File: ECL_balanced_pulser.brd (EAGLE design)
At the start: 40 x 50 mm, 41 parts, among them Q1 BC636, T1 2N2369, U1 MC100EPT22DG, U2 MAX961ESA+, X1 BU-SMA-H, X2 BU-SMA-H, X3 BU-SMA-H

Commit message: added a small copyright note
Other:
- board text added: "Copyright 2015 by Mathias Helsen, MIT license"
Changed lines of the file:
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@@
 <rectangle x1="8.5725" y1="23.8125" x2="12.3825" y2="26.67" layer="41" rot="R180"/>
 <rectangle x1="10.4775" y1="20.32" x2="25.7175" y2="30.1625" layer="42" rot="R180"/>
+<text x="1" y="-4" size="1.778" layer="51">Copyright 2015 by Mathias Helsen, MIT license</text>
 </plain>
 <attributes>
@@
 <polygon width="0.4064" layer="1" isolate="0.3048">
 <vertex x="0" y="0"/>
-<vertex x="78.105" y="0"/>
-<vertex x="77.7875" y="82.55"/>
-<vertex x="0" y="82.55"/>
+<vertex x="41.105" y="0"/>
+<vertex x="40.7875" y="50.55"/>
+<vertex x="0" y="50.55"/>
 </polygon>
 <contactref element="R8" pad="1"/>
@@
 <contactref element="JP3" pad="1"/>
 <polygon width="0.4064" layer="16" isolate="0.3048">
-<vertex x="78.105" y="0"/>
+<vertex x="41.105" y="0"/>
 <vertex x="0" y="0"/>
-<vertex x="0" y="82.55"/>
-<vertex x="77.7875" y="82.55"/>
+<vertex x="0" y="50.55"/>
+<vertex x="40.7875" y="50.55"/>
 </polygon>
 </signal>

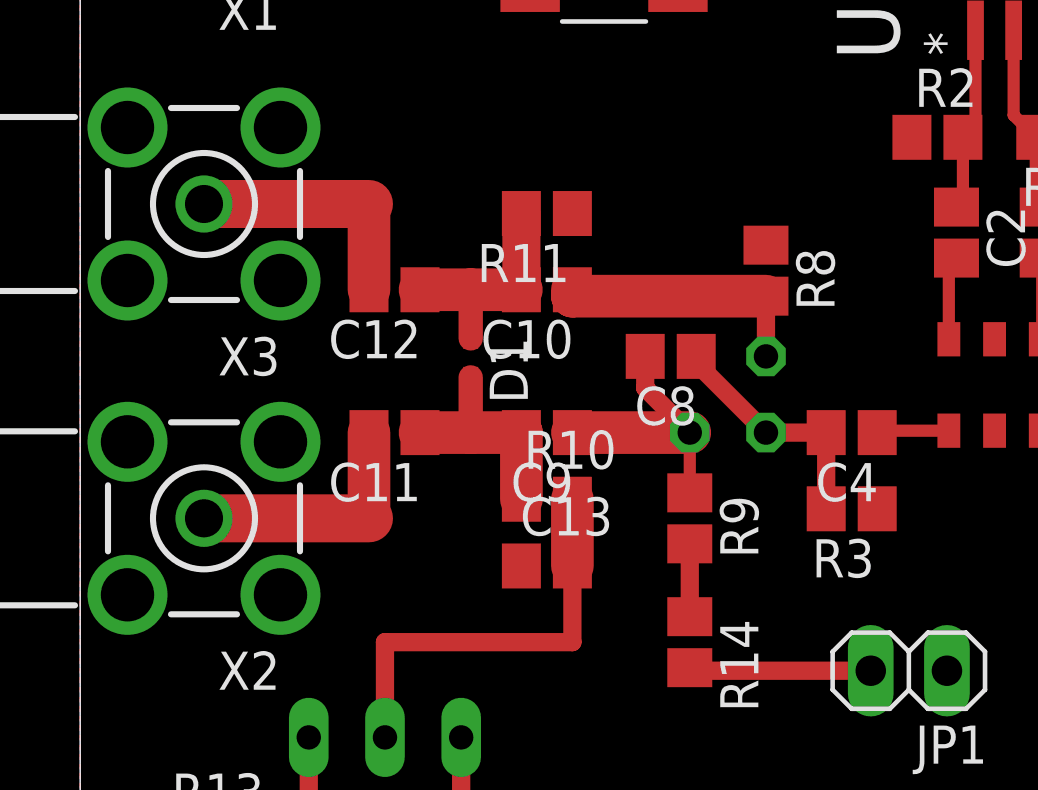
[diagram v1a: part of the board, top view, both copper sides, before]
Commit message: custom footprint for 2D524A SRD
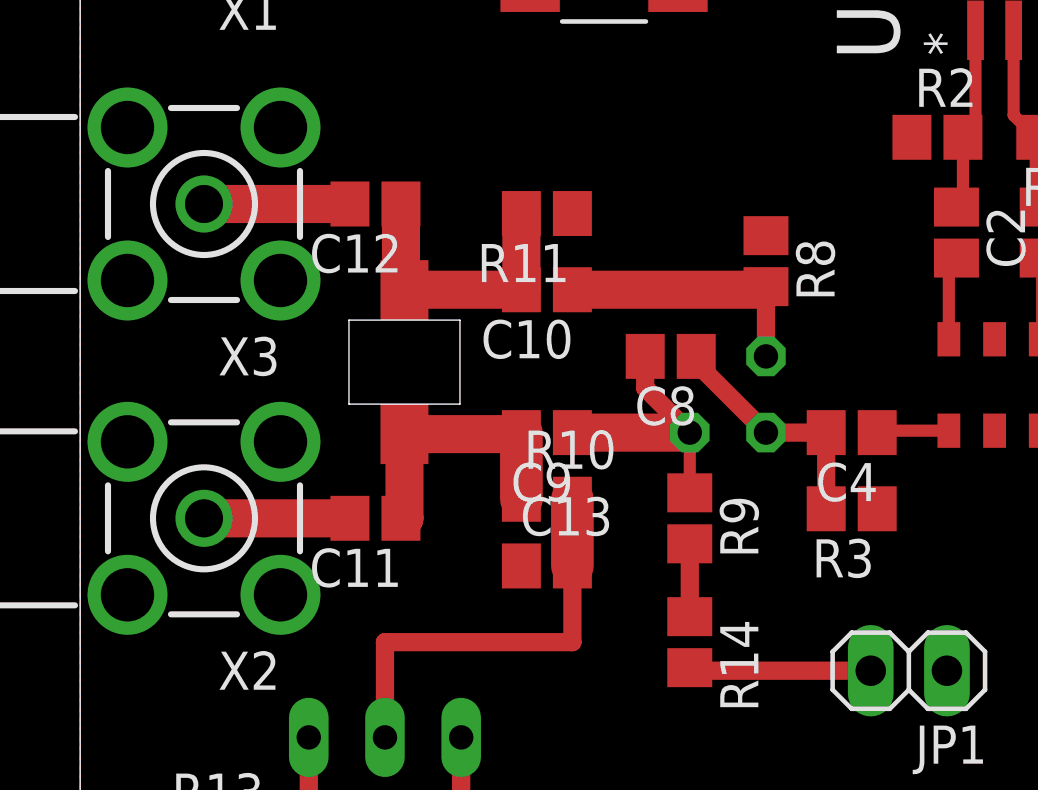
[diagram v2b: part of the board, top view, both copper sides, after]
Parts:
- removed D1: BB141, diode:SOD523
- added U$2: 2D524A, srd:2D524A
- moved C12 2.93 mm to (9.84, 30.5)
- moved C11 2.93 mm to (9.84, 20.0)
- moved R8 0.32 mm to (22.9, 28.6)
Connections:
- net N$14: now also U$2.ANODE; no longer D1.A
- net N$16: now also U$2.CATHODE; no longer D1.C
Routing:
- net N$17: track 8.36 -> 4.86 mm
- net N$15: track 8.36 -> 4.86 mm
- net N$16: track 7.54 -> 9.44 mm
- net N$14: track 7.44 -> 9.09 mm
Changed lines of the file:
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@@
 <setting verticaltext="up"/>
 </settings>
-<grid distance="1" unitdist="mm" unit="mm" style="lines" multiple="1" display="no" altdistance="0.025" altunitdist="inch" altunit="inch"/>
+<grid distance="0.0125" unitdist="inch" unit="inch" style="lines" multiple="1" display="no" altdistance="0.025" altunitdist="inch" altunit="inch"/>
 <layers>
 <layer number="1" name="Top" color="4" fill="1" visible="yes" active="yes"/>
@@
 <layer number="27" name="tValues" color="7" fill="1" visible="yes" active="yes"/>
 <layer number="28" name="bValues" color="7" fill="1" visible="yes" active="yes"/>
-<layer number="29" name="tStop" color="7" fill="3" visible="no" active="yes"/>
-<layer number="30" name="bStop" color="7" fill="6" visible="no" active="yes"/>
-<layer number="31" name="tCream" color="7" fill="4" visible="no" active="yes"/>
-<layer number="32" name="bCream" color="7" fill="5" visible="no" active="yes"/>
-<layer number="33" name="tFinish" color="6" fill="3" visible="no" active="yes"/>
-<layer number="34" name="bFinish" color="6" fill="6" visible="no" active="yes"/>
-<layer number="35" name="tGlue" color="7" fill="4" visible="no" active="yes"/>
-<layer number="36" name="bGlue" color="7" fill="5" visible="no" active="yes"/>
-<layer number="37" name="tTest" color="7" fill="1" visible="no" active="yes"/>
-<layer number="38" name="bTest" color="7" fill="1" visible="no" active="yes"/>
+<layer number="29" name="tStop" color="7" fill="3" visible="yes" active="yes"/>
+<layer number="30" name="bStop" color="7" fill="6" visible="yes" active="yes"/>
+<layer number="31" name="tCream" color="7" fill="4" visible="yes" active="yes"/>
+<layer number="32" name="bCream" color="7" fill="5" visible="yes" active="yes"/>
+<layer number="33" name="tFinish" color="6" fill="3" visible="yes" active="yes"/>
+<layer number="34" name="bFinish" color="6" fill="6" visible="yes" active="yes"/>
+<layer number="35" name="tGlue" color="7" fill="4" visible="yes" active="yes"/>
+<layer number="36" name="bGlue" color="7" fill="5" visible="yes" active="yes"/>
+<layer number="37" name="tTest" color="7" fill="1" visible="yes" active="yes"/>
+<layer number="38" name="bTest" color="7" fill="1" visible="yes" active="yes"/>
 <layer number="39" name="tKeepout" color="4" fill="11" visible="yes" active="yes"/>
 <layer number="40" name="bKeepout" color="1" fill="11" visible="yes" active="yes"/>
@@
 <layer number="42" name="bRestrict" color="1" fill="10" visible="yes" active="yes"/>
 <layer number="43" name="vRestrict" color="2" fill="10" visible="yes" active="yes"/>
-<layer number="44" name="Drills" color="7" fill="1" visible="no" active="yes"/>
-<layer number="45" name="Holes" color="7" fill="1" visible="no" active="yes"/>
-<layer number="46" name="Milling" color="3" fill="1" visible="no" active="yes"/>
-<layer number="47" name="Measures" color="7" fill="1" visible="no" active="yes"/>
+<layer number="44" name="Drills" color="7" fill="1" visible="yes" active="yes"/>
+<layer number="45" name="Holes" color="7" fill="1" visible="yes" active="yes"/>
+<layer number="46" name="Milling" color="3" fill="1" visible="yes" active="yes"/>
+<layer number="47" name="Measures" color="7" fill="1" visible="yes" active="yes"/>
 <layer number="48" name="Document" color="7" fill="1" visible="yes" active="yes"/>
 <layer number="49" name="Reference" color="7" fill="1" visible="yes" active="yes"/>
@@
 <wire x1="40" y1="50" x2="0" y2="50" width="0" layer="20"/>
 <wire x1="0" y1="50" x2="0" y2="0" width="0" layer="20"/>
-<rectangle x1="8.5725" y1="23.8125" x2="12.3825" y2="26.67" layer="41" rot="R180"/>
 <rectangle x1="10.4775" y1="20.32" x2="25.7175" y2="30.1625" layer="42" rot="R180"/>
 <text x="1" y="-4" size="1.778" layer="51">Copyright 2015 by Mathias Helsen, MIT license</text>
@@
 <attribute name="OC_FARNELL" value="unknown" x="4.1275" y="30.48" size="1.778" layer="27" rot="R180" display="off"/>
 </element>
-<element name="R8" library="resistor" package="R0805" value="3k3" x="22.86" y="28.2575" rot="R270"/>
+<element name="R8" library="resistor" package="R0805" value="3k3" x="22.86" y="28.575" rot="R270"/>
 <element name="R9" library="resistor" package="R0805" value="3k3" x="20.32" y="20.0025" rot="R270"/>
 <element name="C8" library="resistor" package="C0805" value="4p8" x="19.685" y="25.4" rot="R180"/>
@@
 <element name="C9" library="resistor" package="C0805" value="180" x="15.5575" y="22.86" rot="R180"/>
 <element name="C10" library="resistor" package="C0805" value="180" x="15.5575" y="27.6225" rot="R180"/>
-<element name="D1" library="diode" package="SOD523" value="BB141" x="13.0175" y="25.4" rot="R270"/>
 <element name="R10" library="resistor" package="R0805" value="39" x="15.5575" y="20.6375"/>
 <element name="R11" library="resistor" package="R0805" value="39" x="15.5575" y="30.1625" rot="R180"/>
-<element name="C11" library="resistor" package="C0805" value="0.001" x="10.4775" y="22.86" rot="R180"/>
-<element name="C12" library="resistor" package="C0805" value="0.001" x="10.4775" y="27.6225" rot="R180"/>
+<element name="C11" library="resistor" package="C0805" value="0.001" x="9.8425" y="20.0025" rot="R180"/>
+<element name="C12" library="resistor" package="C0805" value="0.001" x="9.8425" y="30.48" rot="R180"/>
 <element name="C13" library="resistor" package="C0805" value="" x="15.5575" y="18.415"/>
 <element name="R12" library="pot" package="SP19L" value="" x="10.16" y="5.3975" rot="MR180"/>
@@
 <element name="R15" library="resistor" package="R0805" value="" x="20.32" y="4.1275"/>
 <element name="Q1" library="transistor-pnp" package="TO92-BCE" value="BC636" x="10.16" y="12.7" rot="MR0"/>
+<element name="U$2" library="srd" package="2D524A" value="2D524A" x="10.81" y="25.21" rot="R90"/>
 </elements>
 <signals>
@@
 <contactref element="C9" pad="1"/>
 <wire x1="20.32" y1="22.86" x2="20.32" y2="20.8525" width="0.4064" layer="1"/>
-<wire x1="16.4075" y1="22.86" x2="20.32" y2="22.86" width="1.4224" layer="1"/>
 <wire x1="20.32" y1="22.86" x2="18.835" y2="24.345" width="0.6096" layer="1"/>
 <wire x1="18.835" y1="24.345" x2="18.835" y2="25.4" width="0.6096" layer="1"/>
+<wire x1="16.4075" y1="22.86" x2="20.32" y2="22.86" width="1.27" layer="1"/>
 </signal>
 <signal name="N$12">
@@
 <contactref element="T1" pad="1"/>
 <contactref element="C10" pad="1"/>
-<wire x1="22.86" y1="27.4075" x2="16.4075" y2="27.4075" width="1.4224" layer="1"/>
-<wire x1="16.4075" y1="27.4075" x2="16.4075" y2="27.6225" width="1.4224" layer="1"/>
-<wire x1="22.86" y1="27.4075" x2="22.86" y2="25.4" width="0.6096" layer="1"/>
+<wire x1="22.86" y1="27.725" x2="22.86" y2="25.4" width="0.6096" layer="1"/>
+<wire x1="16.4075" y1="27.6225" x2="22.86" y2="27.6225" width="1.27" layer="1"/>
+<wire x1="22.86" y1="27.6225" x2="22.86" y2="27.725" width="1.27" layer="1"/>
 </signal>
 <signal name="N$14">
 <contactref element="C9" pad="2"/>
 <contactref element="C11" pad="1"/>
-<contactref element="D1" pad="A"/>
 <contactref element="R10" pad="1"/>
-<wire x1="14.7075" y1="22.86" x2="13.0175" y2="22.86" width="1.4224" layer="1"/>
-<wire x1="13.0175" y1="22.86" x2="11.3275" y2="22.86" width="1.4224" layer="1"/>
 <wire x1="14.7075" y1="20.6375" x2="14.7075" y2="22.86" width="1.4224" layer="1"/>
-<wire x1="13.0175" y1="24.7" x2="13.0175" y2="22.86" width="0.8128" layer="1"/>
+<contactref element="U$2" pad="ANODE"/>
+<wire x1="10.6925" y1="20.0025" x2="10.81" y2="20.0025" width="1.27" layer="1"/>
+<wire x1="10.81" y1="20.0025" x2="10.81" y2="22.81" width="1.27" layer="1"/>
+<wire x1="10.81" y1="22.81" x2="14.7075" y2="22.81" width="1.27" layer="1"/>
+<wire x1="14.7075" y1="22.81" x2="14.7075" y2="22.86" width="1.27" layer="1"/>
 </signal>
 <signal name="N$15">
 <contactref element="C11" pad="2"/>
 <contactref element="X2" pad="1"/>
-<wire x1="4.1275" y1="20.0025" x2="9.6275" y2="20.0025" width="1.6" layer="1"/>
-<wire x1="9.6275" y1="20.0025" x2="9.6275" y2="22.86" width="1.4224" layer="1"/>
+<wire x1="4.1275" y1="20.0025" x2="8.9925" y2="20.0025" width="1.27" layer="1"/>
 </signal>
 <signal name="N$16">
 <contactref element="R11" pad="2"/>
-<contactref element="D1" pad="C"/>
 <contactref element="C10" pad="2"/>
 <contactref element="C12" pad="1"/>
-<wire x1="14.7075" y1="27.6225" x2="13.0175" y2="27.6225" width="1.4224" layer="1"/>
-<wire x1="13.0175" y1="27.6225" x2="11.3275" y2="27.6225" width="1.4224" layer="1"/>
-<wire x1="13.0175" y1="26" x2="13.0175" y2="27.6225" width="0.8128" layer="1"/>
 <wire x1="14.7075" y1="30.1625" x2="14.7075" y2="27.6225" width="1.27" layer="1"/>
+<contactref element="U$2" pad="CATHODE"/>
+<wire x1="14.7075" y1="27.6225" x2="10.81" y2="27.6225" width="1.27" layer="1"/>
+<wire x1="10.81" y1="27.6225" x2="10.81" y2="27.61" width="1.27" layer="1"/>
+<wire x1="10.81" y1="27.61" x2="10.6925" y2="27.61" width="1.27" layer="1"/>
+<wire x1="10.6925" y1="27.61" x2="10.6925" y2="30.48" width="1.27" layer="1"/>
 </signal>
 <signal name="N$17">
 <contactref element="C12" pad="2"/>
 <contactref element="X3" pad="1"/>
-<wire x1="4.1275" y1="30.48" x2="9.6275" y2="30.48" width="1.6" layer="1"/>
-<wire x1="9.6275" y1="30.48" x2="9.6275" y2="27.6225" width="1.4224" layer="1"/>
+<wire x1="4.1275" y1="30.48" x2="8.9925" y2="30.48" width="1.27" layer="1"/>
 </signal>
 <signal name="N$18">
